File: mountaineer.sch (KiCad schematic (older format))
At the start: 69 parts, among them J1 USB_C_Receptacle, J2 CAT, J3 AUDIO, SW1 VCCIO, U1 TUSB2036, U2 FT232RL, U3 HS-100B, U4 TPS76333, U5 SN75240, U6 TPS2041, Y1 AWSCR-6.00CPLA

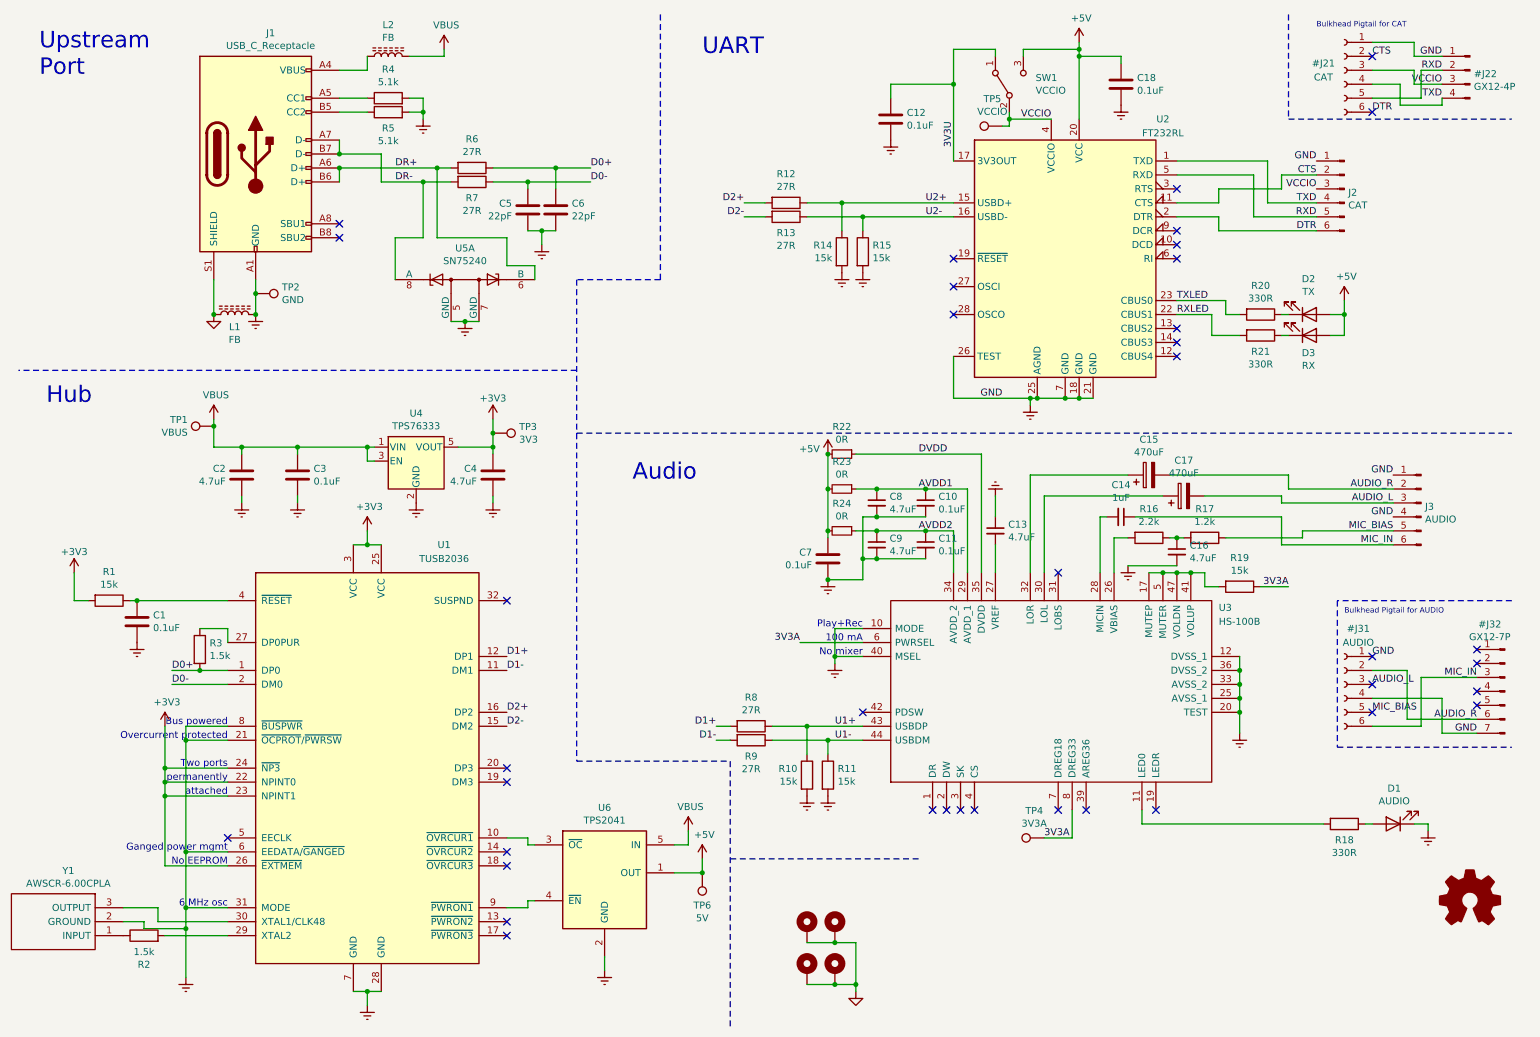
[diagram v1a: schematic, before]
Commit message: Add pullup resistor to overcurrent protection
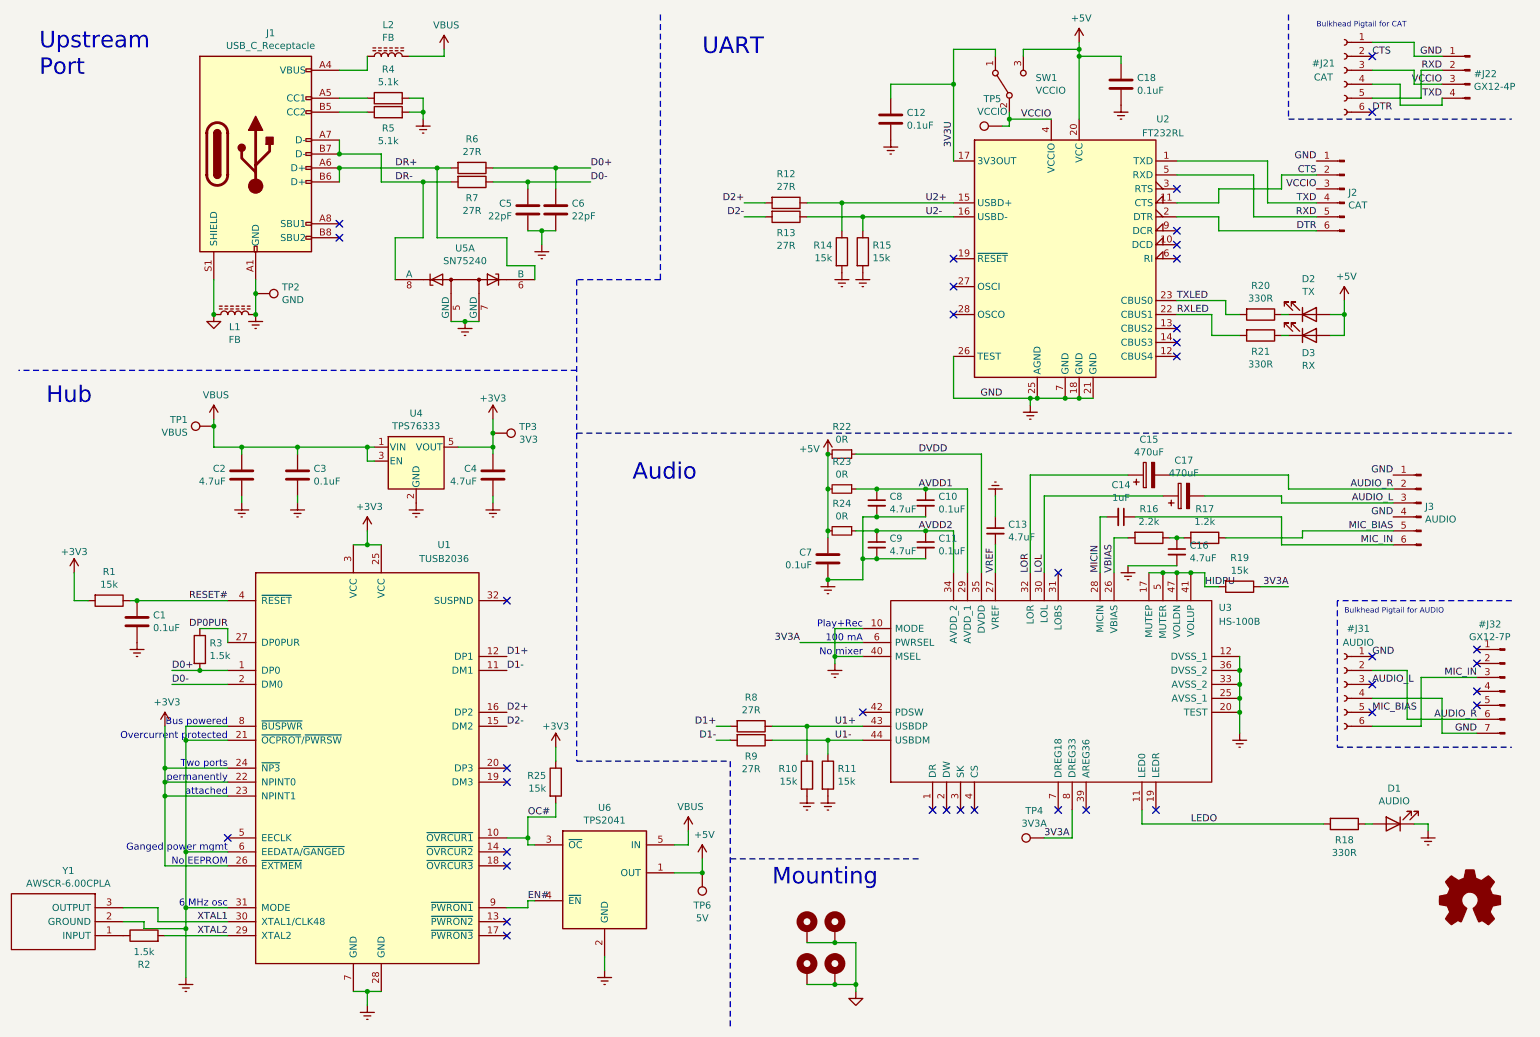
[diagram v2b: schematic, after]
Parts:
- added R25: 15k, Resistor_SMD:R_0603_1608Metric, symbol Device:R
- SW1: Vendor Mouser -> Newark; Vendor Part Number 611-JS102011SAQN -> 35AH0889
- U1: Description USB Hub Controller -> (none); Vendor Mouser -> Digikey; Vendor Part Number 595-TUSB2036VFRG4 -> 296-27129-1-ND
- U2: Description UART -> (none)
- U3: Description USB Audio Interface -> (none)
- U4: Description Voltage Regulator -> (none)
- U5: Description ESD protection -> (none)
- U6: Description Overcurrent protection -> (none)
- Y1: Description Resonator 6 MHz -> (none); Vendor Mouser -> Newark; Vendor Part Number 815-CR-6.00CPLA-30-T -> 16AH0979
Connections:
- net +3V3: now also R25.1
- net OC#: now reaches U1.10 (~OVRCUR1), U6.3 (~OC)
- net OC#: now also R25.2
- net DP0PUR: now reaches R3.1, U1.27 (DP0PUR)
- net XTAL2: now reaches R2.2, U1.29 (XTAL2)
- net XTAL1: now reaches U1.30 (XTAL1/CLK48), Y1.3 (OUTPUT)
- net RESET#: now reaches C1.1, R1.1, U1.4 (~RESET)
- net EN#: now reaches U1.9 (~PWRON1), U6.4 (~EN)
- net LEDO: now reaches R18.2, U3.11 (LED0)
- net HIDPU: now reaches R19.2, U3.17 (MUTEP), U3.41 (VOLUP), U3.47 (VOLDN), U3.5 (MUTER)
- net VBIAS: now reaches R16.2, U3.26 (VBIAS)
- net VREF: now reaches C13.2, U3.27 (VREF)
- net MICIN: now reaches C14.2, U3.28 (MICIN)
- net LOL: now reaches C17.1, U3.30 (LOL)
- net LOR: now reaches C15.1, U3.32 (LOR)
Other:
- note added: "Mounting"

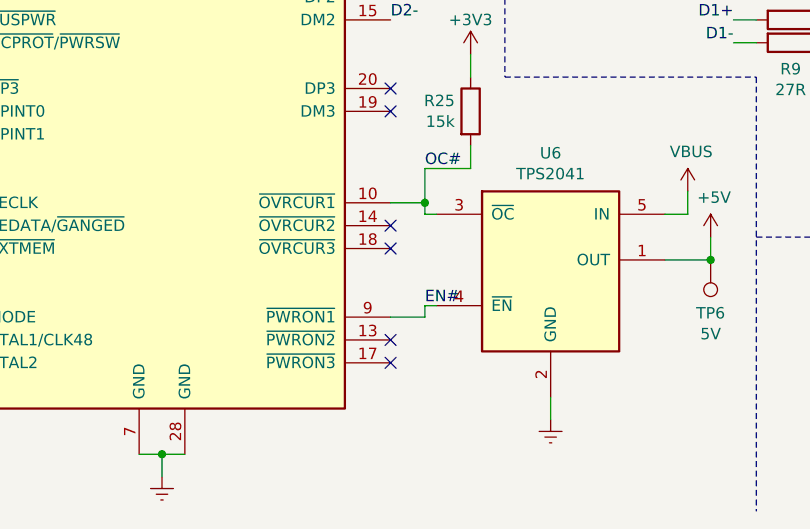
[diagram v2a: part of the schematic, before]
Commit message: Join all Enable and Overcurrent signals
I think this is the problem that has been bothering me for several weeks. When I replaced the TPS2044B with the TPS2041B, I thought I could use any Enable and any Overcurrent signal, but in that configuration the hub would refuse to power on the downstream ports. After testing this with a breadboard, I think this is the solution.
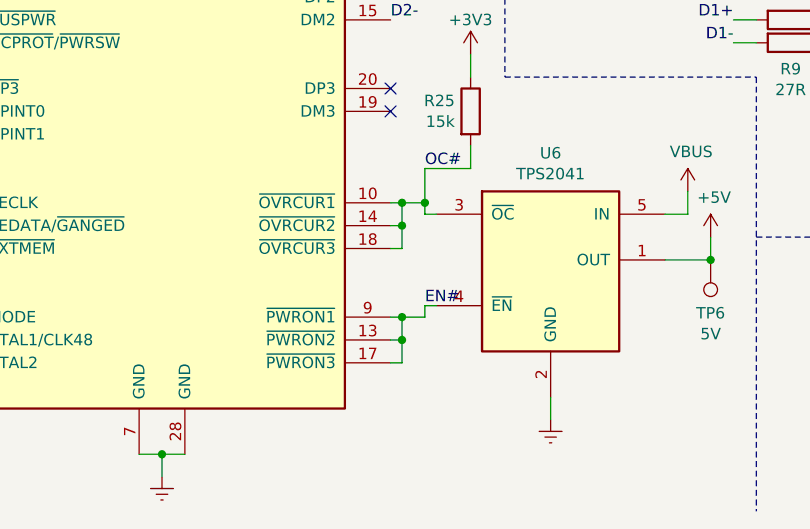
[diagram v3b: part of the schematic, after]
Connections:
- net EN#: now also U1.13 (~PWRON2), U1.17 (~PWRON3)
- net OC#: now also U1.14 (~OVRCUR2), U1.18 (~OVRCUR3)
- no-connect marks 38 -> 34
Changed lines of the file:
@@
 Sheet 1 1
 Title "Mountaineer Radio Interface"
-Date "2021-05-15"
+Date "2021-05-24"
 Rev "2"
 Comp "Chris Keller K0SWE"
@@
 	4350 1600 4600 1600
 Wire Wire Line
-	4000 6900 4150 6900
+	4000 6900 4050 6900
 Wire Wire Line
 	4150 6900 4150 6850
@@
 	4150 6850 4200 6850
 Wire Wire Line
-	4000 6400 4150 6400
+	4000 6400 4050 6400
 Wire Wire Line
 	4150 6400 4150 6450
@@
 NoConn ~ 7950 4500
 NoConn ~ 6550 5500
-NoConn ~ 4000 6500
-NoConn ~ 4000 6600
-NoConn ~ 4000 7000
-NoConn ~ 4000 7100
 NoConn ~ 4000 5900
 NoConn ~ 4000 6000
@@
 NoConn ~ 10200 5500
 NoConn ~ 10200 5300
+Wire Wire Line
+	4050 6400 4050 6500
+Wire Wire Line
+	4050 6500 4000 6500
+Connection ~ 4050 6400
+Wire Wire Line
+	4050 6400 4150 6400
+Wire Wire Line
+	4050 6500 4050 6600
+Wire Wire Line
+	4050 6600 4000 6600
+Connection ~ 4050 6500
+Wire Wire Line
+	4050 6900 4050 7000
+Wire Wire Line
+	4050 7000 4000 7000
+Connection ~ 4050 6900
+Wire Wire Line
+	4050 6900 4150 6900
+Wire Wire Line
+	4050 7000 4050 7100
+Wire Wire Line
+	4050 7100 4000 7100
+Connection ~ 4050 7000
 $EndSCHEMATC

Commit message: Remove VCCIO switch and add more test points
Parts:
- added TP7: EN#, TestPoint:TestPoint_Pad_D1.0mm, symbol Connector:TestPoint
- JP1: renamed from SW1; footprint Button_Switch_SMD:SW_SPDT_CK-JS102011SAQN -> Jumper:SolderJumper-3_P1.3mm_Bridged12_RoundedPad1.0x1.5mm; symbol Switch:SW_SPDT -> Jumper:Jumper_3_Bridged12; LCSC C221660 -> (none); Manufacturer_Name C&K -> (none); Manufacturer_Part_Number JS102011SAQN -> (none); Vendor Newark -> (none); Vendor Part Number 35AH0889 -> (none)
- R18: value 330R -> 68R; LCSC C23137 -> C27592; Vendor Part Number C23137 -> C27592
- R20, R21: value 330R -> 150R; LCSC C23137 -> C22808; Vendor Part Number C23137 -> C22808
- TP5: value VCCIO -> OC#
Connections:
- net EN#: now also TP7.1
- net OC#: now also TP5.1
- net VCCIO: no longer TP5.1
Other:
- moved on the sheet: R7
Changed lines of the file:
@@
 Sheet 1 1
 Title "Mountaineer Radio Interface"
-Date "2021-05-24"
+Date "2021-05-25"
 Rev "2"
 Comp "Chris Keller K0SWE"
@@
 AR Path="/6057976E/6055B627" Ref="R?"  Part="1"
 AR Path="/6055B627" Ref="R6"  Part="1"
-F 0 "R6" V 3543 1600 50  0000 C CNN
-F 1 "27R" V 3634 1600 50  0000 C CNN
+F 0 "R6" V 3865 1600 50  0000 C CNN
+F 1 "27R" V 3956 1600 50  0000 C CNN
 F 2 "Resistor_SMD:R_0603_1608Metric" V 3680 1600 50  0001 C CNN
 F 3 "" H 3750 1600 50  0001 C CNN
@@
 L Device:R R?
 U 1 1 6055B632
-P 3750 1700
+P 3750 1500
 AR Path="/6057976E/6055B632" Ref="R?"  Part="1"
 AR Path="/6055B632" Ref="R7"  Part="1"
-F 0 "R7" V 3865 1700 50  0000 C CNN
-F 1 "27R" V 3956 1700 50  0000 C CNN
-F 2 "Resistor_SMD:R_0603_1608Metric" V 3680 1700 50  0001 C CNN
-F 3 "" H 3750 1700 50  0001 C CNN
-F 4 "C25190" H 3750 1700 50  0001 C CNN "LCSC"
-F 5 "C25190" H 3865 1800 50  0001 C CNN "Vendor Part Number"
-F 6 "LCSC" H 3865 1800 50  0001 C CNN "Vendor"
-	1    3750 1700
+F 0 "R7" V 3543 1500 50  0000 C CNN
+F 1 "27R" V 3634 1500 50  0000 C CNN
+F 2 "Resistor_SMD:R_0603_1608Metric" V 3680 1500 50  0001 C CNN
+F 3 "" H 3750 1500 50  0001 C CNN
+F 4 "C25190" H 3750 1500 50  0001 C CNN "LCSC"
+F 5 "C25190" H 3865 1600 50  0001 C CNN "Vendor Part Number"
+F 6 "LCSC" H 3865 1600 50  0001 C CNN "Vendor"
+	1    3750 1500
 	0    1    1    0
 $EndComp
@@
 $EndComp
 $Comp
-L Switch:SW_SPDT SW1
-U 1 1 61339D80
-P 7600 1000
-F 0 "SW1" V 7646 812 50  0000 R CNN
-F 1 "VCCIO" V 7555 812 50  0000 R CNN
-F 2 "Button_Switch_SMD:SW_SPDT_CK-JS102011SAQN" H 7600 1000 50  0001 C CNN
-F 3 "https://www.ckswitches.com/media/1422/js.pdf" H 7600 1000 50  0001 C CNN
-F 4 "C221660" H 7600 1000 50  0001 C CNN "LCSC"
-F 5 "C&K" H 7646 912 50  0001 C CNN "Manufacturer_Name"
-F 6 "JS102011SAQN" H 7646 912 50  0001 C CNN "Manufacturer_Part_Number"
-F 7 "35AH0889" H 7646 912 50  0001 C CNN "Vendor Part Number"
-F 8 "Newark" H 7646 912 50  0001 C CNN "Vendor"
-	1    7600 1000
-	0    -1   -1   0
-$EndComp
-$Comp
 L Device:LED D2
 U 1 1 6138837F
@@
 P 9400 2650
 F 0 "R20" V 9193 2650 50  0000 C CNN
-F 1 "330R" V 9284 2650 50  0000 C CNN
+F 1 "150R" V 9284 2650 50  0000 C CNN
 F 2 "Resistor_SMD:R_0603_1608Metric" V 9330 2650 50  0001 C CNN
 F 3 "" H 9400 2650 50  0001 C CNN
-F 4 "C23137" H 9400 2650 50  0001 C CNN "LCSC"
-F 5 "C23137" H 9193 2750 50  0001 C CNN "Vendor Part Number"
+F 4 "C22808" H 9400 2650 50  0001 C CNN "LCSC"
+F 5 "C22808" H 9193 2750 50  0001 C CNN "Vendor Part Number"
 F 6 "LCSC" H 9193 2750 50  0001 C CNN "Vendor"
 	1    9400 2650
@@
 P 9400 2800
 F 0 "R21" V 9515 2800 50  0000 C CNN
-F 1 "330R" V 9606 2800 50  0000 C CNN
+F 1 "150R" V 9606 2800 50  0000 C CNN
 F 2 "Resistor_SMD:R_0603_1608Metric" V 9330 2800 50  0001 C CNN
 F 3 "" H 9400 2800 50  0001 C CNN
-F 4 "C23137" H 9400 2800 50  0001 C CNN "LCSC"
-F 5 "C23137" H 9515 2900 50  0001 C CNN "Vendor Part Number"
+F 4 "C22808" H 9400 2800 50  0001 C CNN "LCSC"
+F 5 "C22808" H 9515 2900 50  0001 C CNN "Vendor Part Number"
 F 6 "LCSC" H 9515 2900 50  0001 C CNN "Vendor"
 	1    9400 2800
@@
 P 10000 6300
 F 0 "R18" V 10115 6300 50  0000 C CNN
-F 1 "330R" V 10206 6300 50  0000 C CNN
+F 1 "68R" V 10206 6300 50  0000 C CNN
 F 2 "Resistor_SMD:R_0603_1608Metric" V 9930 6300 50  0001 C CNN
 F 3 "" H 10000 6300 50  0001 C CNN
-F 4 "C23137" H 10000 6300 50  0001 C CNN "LCSC"
-F 5 "C23137" H 10115 6400 50  0001 C CNN "Vendor Part Number"
+F 4 "C27592" H 10000 6300 50  0001 C CNN "LCSC"
+F 5 "C27592" H 10115 6400 50  0001 C CNN "Vendor Part Number"
 F 6 "LCSC" H 10115 6400 50  0001 C CNN "Vendor"
 	1    10000 6300
@@
 $EndComp
 $Comp
-L Connector:TestPoint TP5
-U 1 1 6096374D
-P 7550 1300
-F 0 "TP5" V 7745 1372 50  0000 C CNN
-F 1 "VCCIO" V 7654 1372 50  0000 C CNN
-F 2 "TestPoint:TestPoint_Pad_D1.0mm" H 7750 1300 50  0001 C CNN
-F 3 "-" H 7750 1300 50  0001 C CNN
-F 4 "-" H 7550 1300 50  0001 C CNN "LCSC"
-F 5 "-" H 7745 1472 50  0001 C CNN "Manufacturer_Name"
-F 6 "-" H 7745 1472 50  0001 C CNN "Manufacturer_Part_Number"
-F 7 "-" H 7745 1472 50  0001 C CNN "Vendor Part Number"
-F 8 "-" H 7745 1472 50  0001 C CNN "Vendor"
-	1    7550 1300
-	0    -1   -1   0
-$EndComp
-$Comp
 L Connector:TestPoint TP6
 U 1 1 6098B958
@@
 Text Label 3200 1600 0    50   ~ 0
 DR+
-Text Label 3200 1700 0    50   ~ 0
+Text Label 3200 1500 0    50   ~ 0
 DR-
 Text Label 9800 1750 2    50   ~ 0
@@
 Text Label 4600 1600 0    50   ~ 0
 D0+
-Text Label 4600 1700 0    50   ~ 0
+Text Label 4600 1500 0    50   ~ 0
 D0-
 Text Notes 650  950  0    118  ~ 0
@@
 	4350 1750 4350 1600
 Wire Wire Line
-	4150 1700 4150 1750
+	4150 1500 4150 1750
 Wire Wire Line
 	8400 800  8400 850
@@
 	3500 1600 3600 1600
 Wire Wire Line
-	3400 1700 3400 2100
+	3400 1500 3400 2100
 Wire Wire Line
 	3400 2100 3200 2100
@@
 	3200 2100 3200 2400
 Wire Wire Line
-	3400 1700 3600 1700
-Wire Wire Line
 	3600 2700 3700 2700
 Wire Wire Line
@@
 	5500 5600 5600 5600
 Wire Wire Line
-	8100 800  8100 1250
+	8100 800  8100 1000
 Wire Wire Line
 	1900 3400 1900 3450
@@
 	3900 1600 4350 1600
 Wire Wire Line
-	3900 1700 4150 1700
+	3900 1500 4150 1500
 Wire Wire Line
 	1350 4700 2000 4700
@@
 	7900 1250 7600 1250
 Wire Wire Line
-	7600 1250 7600 1200
-Wire Wire Line
-	7500 750  7200 750
-Wire Wire Line
-	7200 750  7200 1000
-Wire Wire Line
-	8100 700  8100 750
-Wire Wire Line
-	7500 750  7500 800
-Wire Wire Line
-	7700 800  7700 750
-Wire Wire Line
-	7700 750  8100 750
-Wire Wire Line
-	8100 750  8100 800
-Wire Wire Line
 	10000 2550 10000 2650
 Wire Wire Line
@@
 	1600 5300 2000 5300
 Wire Wire Line
-	4600 1700 4150 1700
+	4600 1500 4150 1500
 Wire Wire Line
 	4350 1600 4600 1600
@@
 	2800 1400 2800 1500
 Wire Wire Line
-	2800 1500 3100 1500
-Wire Wire Line
-	3100 1500 3100 1700
-Wire Wire Line
-	3100 1700 3400 1700
-Wire Wire Line
 	2800 1700 2800 1600
 Wire Wire Line
@@
 Wire Wire Line
 	1700 7050 1700 7400
-Wire Wire Line
-	7600 1250 7600 1300
-Wire Wire Line
-	7600 1300 7550 1300
 Wire Wire Line
 	6500 3650 7400 3650
@@
 Connection ~ 3900 3500
 Connection ~ 3500 1600
-Connection ~ 3400 1700
 Connection ~ 1550 6000
 Connection ~ 1700 6500
@@
 Connection ~ 1900 2650
 Connection ~ 2200 2650
-Connection ~ 7200 1000
-Connection ~ 8100 750
 Connection ~ 10000 2650
 Connection ~ 8800 4500
@@
 Connection ~ 8900 4500
 Connection ~ 1800 5200
-Connection ~ 4150 1700
+Connection ~ 4150 1500
 Connection ~ 4350 1600
 Connection ~ 2800 1500
@@
 Connection ~ 1700 6900
 Connection ~ 1700 7050
-Connection ~ 7600 1250
 Connection ~ 5400 6650
 Connection ~ 6350 7150
@@
 	4050 7100 4000 7100
 Connection ~ 4050 7000
+$Comp
+L Jumper:Jumper_3_Bridged12 JP1
+U 1 1 61339D80
+P 7600 1000
+F 0 "JP1" H 7600 1204 50  0000 C CNN
+F 1 "VCCIO" H 7600 1113 50  0000 C CNN
+F 2 "Jumper:SolderJumper-3_P1.3mm_Bridged12_RoundedPad1.0x1.5mm" H 7600 1000 50  0001 C CNN
+F 3 "-" H 7600 1000 50  0001 C CNN
+	1    7600 1000
+	1    0    0    -1
+$EndComp
+Wire Wire Line
+	8100 700  8100 800
+Wire Wire Line
+	7600 1150 7600 1250
+Wire Wire Line
+	7850 1000 8100 1000
+Connection ~ 8100 1000
+Wire Wire Line
+	8100 1000 8100 1250
+Wire Wire Line
+	7350 1000 7200 1000
+Connection ~ 7200 1000
+Wire Wire Line
+	3600 1500 3400 1500
+Connection ~ 3400 1500
+Wire Wire Line
+	2800 1500 3400 1500
+$Comp
+L Connector:TestPoint TP7
+U 1 1 60C3EEF4
+P 4150 6900
+F 0 "TP7" H 4092 6926 50  0000 R CNN
+F 1 "EN#" H 4092 7017 50  0000 R CNN
+F 2 "TestPoint:TestPoint_Pad_D1.0mm" H 4350 6900 50  0001 C CNN
+F 3 "-" H 4350 6900 50  0001 C CNN
+F 4 "-" H 4150 6900 50  0001 C CNN "LCSC"
+F 5 "-" H 4150 7233 50  0001 C CNN "Manufacturer_Name"
+F 6 "-" H 4150 7233 50  0001 C CNN "Manufacturer_Part_Number"
+F 7 "-" H 4150 7233 50  0001 C CNN "Vendor Part Number"
+F 8 "-" H 4150 7233 50  0001 C CNN "Vendor"
+	1    4150 6900
+	-1   0    0    1
+$EndComp
+$Comp
+L Connector:TestPoint TP5
+U 1 1 60C4050B
+P 4150 6450
+F 0 "TP5" H 4092 6476 50  0000 R CNN
+F 1 "OC#" H 4092 6567 50  0000 R CNN
+F 2 "TestPoint:TestPoint_Pad_D1.0mm" H 4350 6450 50  0001 C CNN
+F 3 "-" H 4350 6450 50  0001 C CNN
+F 4 "-" H 4150 6450 50  0001 C CNN "LCSC"
+F 5 "-" H 4150 6783 50  0001 C CNN "Manufacturer_Name"
+F 6 "-" H 4150 6783 50  0001 C CNN "Manufacturer_Part_Number"
+F 7 "-" H 4150 6783 50  0001 C CNN "Vendor Part Number"
+F 8 "-" H 4150 6783 50  0001 C CNN "Vendor"
+	1    4150 6450
+	-1   0    0    1
+$EndComp
+Connection ~ 4150 6900
+Connection ~ 4150 6450
 $EndSCHEMATC

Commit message: Switch audio from HS100B to CM108B
The HS-100B is getting hard to find, but the CM108B is still available.
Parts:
- U3: value HS-100B -> CM108B; symbol HS-100B:HS-100B -> cmedia:CM-108B; LCSC C371351 -> C371347; Manufacturer_Part_Number HS-100B -> CM108B; Vendor Part Number HS-100B -> CM108B
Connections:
- net 3V3A: now also U3.7 (PWRSEL), U3.9 (DREG33); no longer U3.6 (PWRSEL), U3.8 (DREG33)
- net GNDREF: now also U3.14 (DVSS_1), U3.23 (TEST), U3.24 (AVSS_1), U3.38 (MSEL); no longer U3.12 (DVSS_1), U3.20 (TEST), U3.25 (AVSS_1), U3.40 (MSEL)
- net HIDPU: now also U3.18 (MUTEP), U3.39 (VOLUP), U3.48 (VOLDN), U3.6 (MUTER); no longer U3.17 (MUTEP), U3.41 (VOLUP), U3.47 (VOLDN), U3.5 (MUTER)
- net LEDO: now also U3.12 (LED0); no longer U3.11 (LED0)
- net MICIN: now also U3.27 (MICIN); no longer U3.28 (MICIN)
- net U1+: now also U3.41 (USBDP); no longer U3.43 (USBDP)
- net U1-: now also U3.42 (USBDM); no longer U3.44 (USBDM)
- net VBIAS: now also U3.25 (VBIAS); no longer U3.26 (VBIAS)
- net VREF: now also U3.26 (VREF); no longer U3.27 (VREF)
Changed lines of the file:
@@
 Sheet 1 1
 Title "Mountaineer Radio Interface"
-Date "2021-05-25"
-Rev "2"
+Date "2021-06-06"
+Rev "3"
 Comp "Chris Keller K0SWE"
 Comment1 "Licensed under Creative Commons CC-BY-4.0"
@@
 $EndComp
 $Comp
-L HS-100B:HS-100B U3
+L cmedia:CM-108B U3
 U 1 1 60A2B59C
 P 7350 6200
@@
 AR Path="/605AB33C/60A2B59C" Ref="U?"  Part="1"
 F 0 "U3" V 8800 4450 50  0000 R CNN
-F 1 "HS-100B" V 8700 4450 50  0000 R CNN
+F 1 "CM108B" V 8700 4450 50  0000 R CNN
 F 2 "Package_QFP:LQFP-48_7x7mm_P0.5mm" H 8900 6800 50  0001 L CNN
-F 3 "https://datasheet.lcsc.com/szlcsc/1906061502_Cmedia-HS-100B_C371351.pdf" H 8900 6700 50  0001 L CNN
-F 4 "C371351" H 7350 6200 50  0001 C CNN "LCSC"
+F 3 "https://www.cmedia.com.tw/support/download_center?type=497_datasheet" H 8900 6700 50  0001 L CNN
+F 4 "C371347" H 7350 6200 50  0001 C CNN "LCSC"
 F 5 "Cmedia" H 8900 6400 50  0001 L CNN "Manufacturer_Name"
-F 6 "HS-100B" H 8900 6300 50  0001 L CNN "Manufacturer_Part_Number"
-F 7 "HS-100B" H 8571 4356 50  0001 C CNN "Vendor Part Number"
+F 6 "CM108B" H 8900 6300 50  0001 L CNN "Manufacturer_Part_Number"
+F 7 "CM108B" H 8571 4356 50  0001 C CNN "Vendor Part Number"
 F 8 "Symmetry" H 8571 4356 50  0001 C CNN "Vendor"
 	1    7350 6200
